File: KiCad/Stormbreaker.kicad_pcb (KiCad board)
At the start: 4 copper layers, 50.2 x 21 mm, 50 parts, among them J1 Micro_SD_Card_Det2, J2 USB_C_Receptacle_USB2.0_14P, J3 Conn_01x03, J4 FAN, J5 Conn_01x02, Q1 PMOS, Q2 NMOS, SW1 SW_Push, U1 BQ25895RTW, U3 ATtiny1616-M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

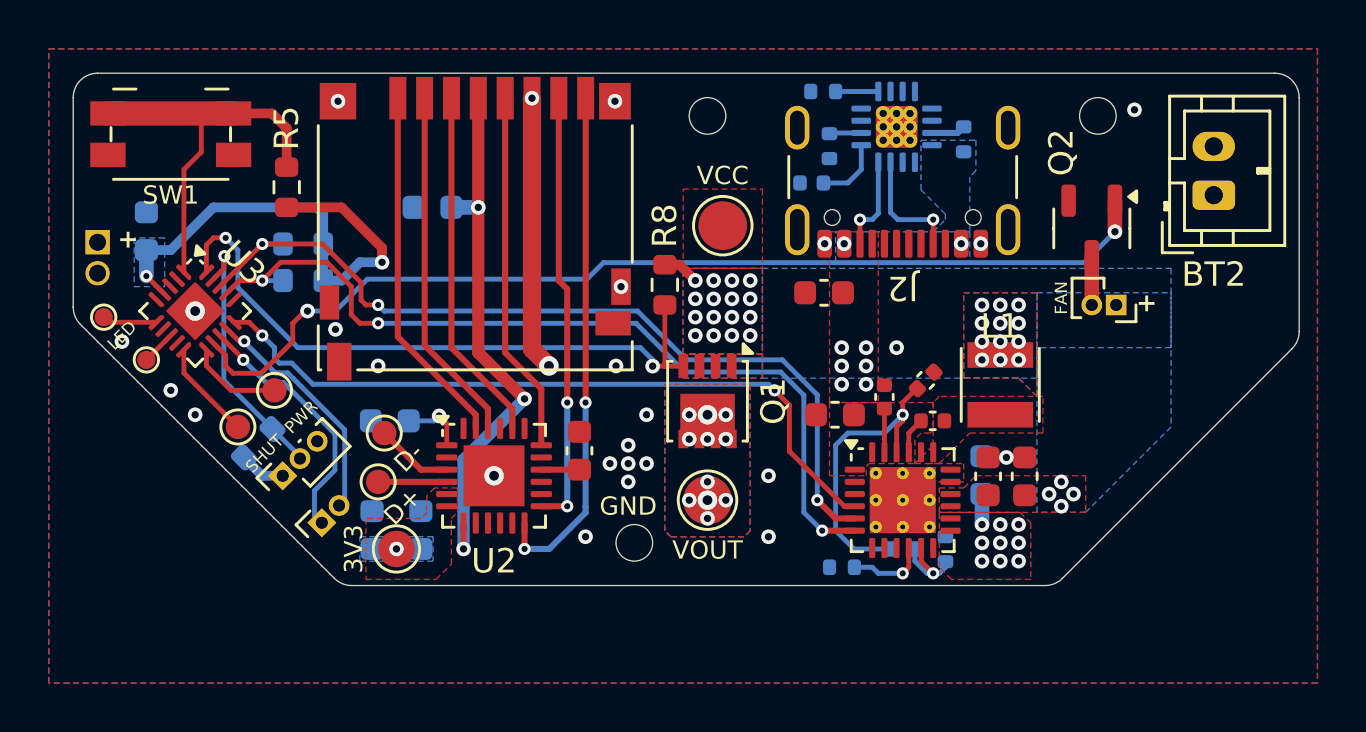
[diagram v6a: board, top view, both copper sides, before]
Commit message: Teardropped pads, slight footprint adjustments
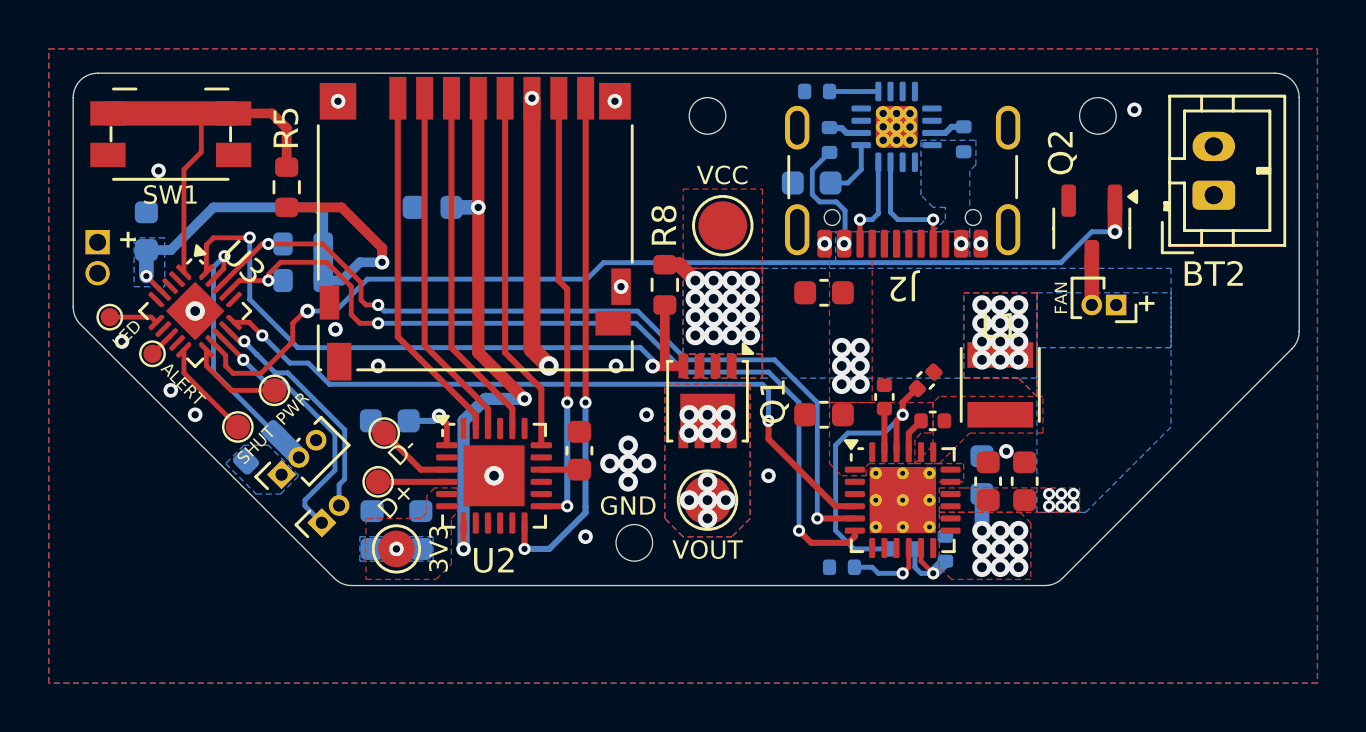
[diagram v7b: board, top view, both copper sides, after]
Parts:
- C15: footprint Capacitor_SMD:C_0402_1005Metric -> Capacitor_SMD:C_0603_1608Metric
- TP1, TP2, TP6, TP7: footprint TestPoint:TestPoint_Pad_D1.0mm -> Stormbreaker:TestPoint_Pad_D1.0mm_Small
- TP10, TP11: footprint TestPoint:TestPoint_Pad_D1.0mm -> Stormbreaker:TestPoint_Pad_D0.75mm_Small
- moved C1 0.45 mm to (144.8, 55.0)
- moved TP11 0.35 mm to (117.2, 52.5), turned to 45 degrees
- moved R12 0.25 mm to (144.5, 41.8)
- moved R6 0.25 mm to (145.0, 43.7)
- moved TP10 0.25 mm to (115.5, 51.0), turned to 45 degrees
- moved C5 0.20 mm to (151.5, 57.7)
- moved C6 0.20 mm to (153.0, 57.7)
- moved R7 0.19 mm to (121.7, 56.3)
- moved J3 0.06 mm to (122.5, 57.5)
- turned C15 to 0 degrees
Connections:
- C15 pad 1: Net-(U4-VDD) -> GND
- C15 pad 2: GND -> Net-(U4-VDD)
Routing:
- net VBUS: track 0.10 -> 5.11 mm
- net VCC: track 24.2 -> 22.3 mm, vias 34 -> 36
- net SD_VCC: track 22.5 -> 23.4 mm
- net SDA_2: track 35.1 -> 35.9 mm
- net Net-(Q1-G): track 26.5 -> 27.1 mm
- net GND: vias 27 -> 26
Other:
- board text removed: "LED"

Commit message: Minor track changes
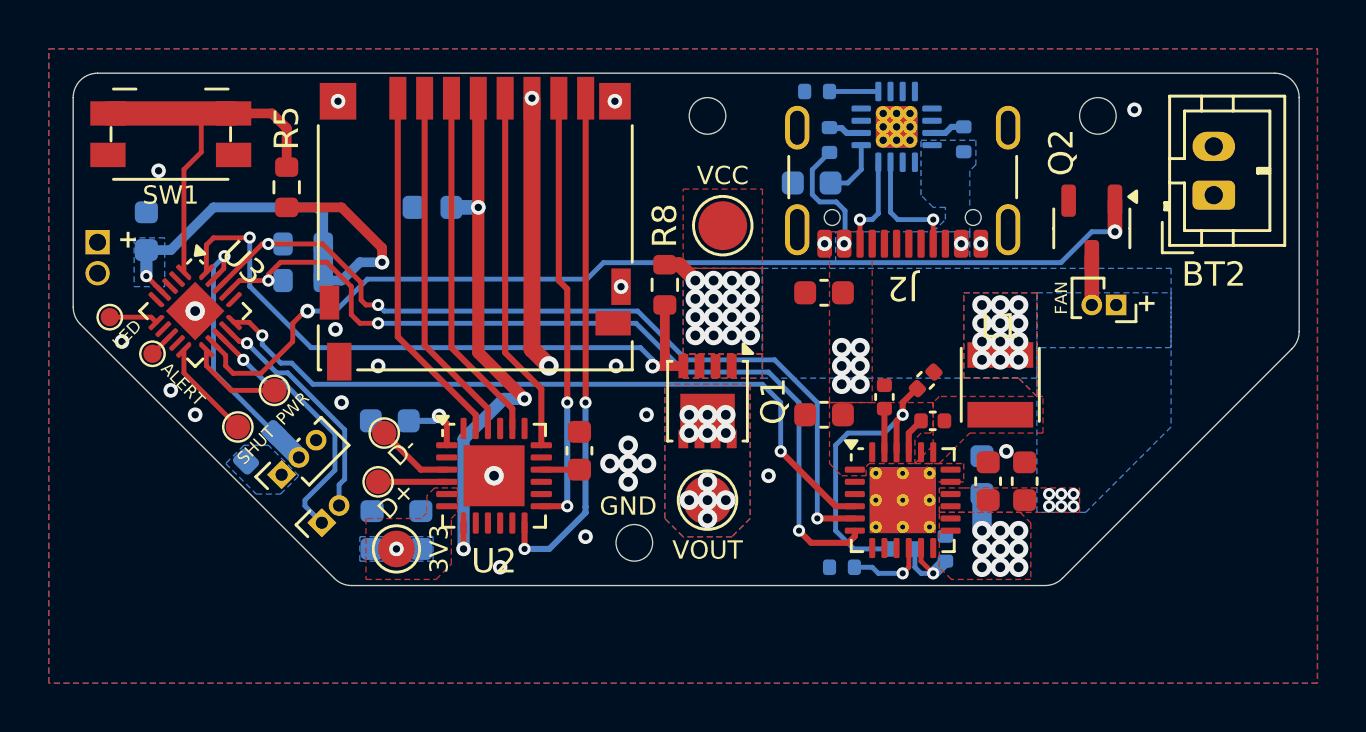
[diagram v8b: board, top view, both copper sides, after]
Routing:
- net GND: vias 26 -> 28
